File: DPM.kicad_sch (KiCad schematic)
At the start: 43 parts, among them J1 Conn_02x12_Odd_Even, J2 Conn_02x05_Odd_Even, U1 74LS251, U2 74LVC2G74, U25 74LS85, U28 74LS85, U3 ADG333A, U31 74LS85, U4 MCP23017_SP, U5 ADG333A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

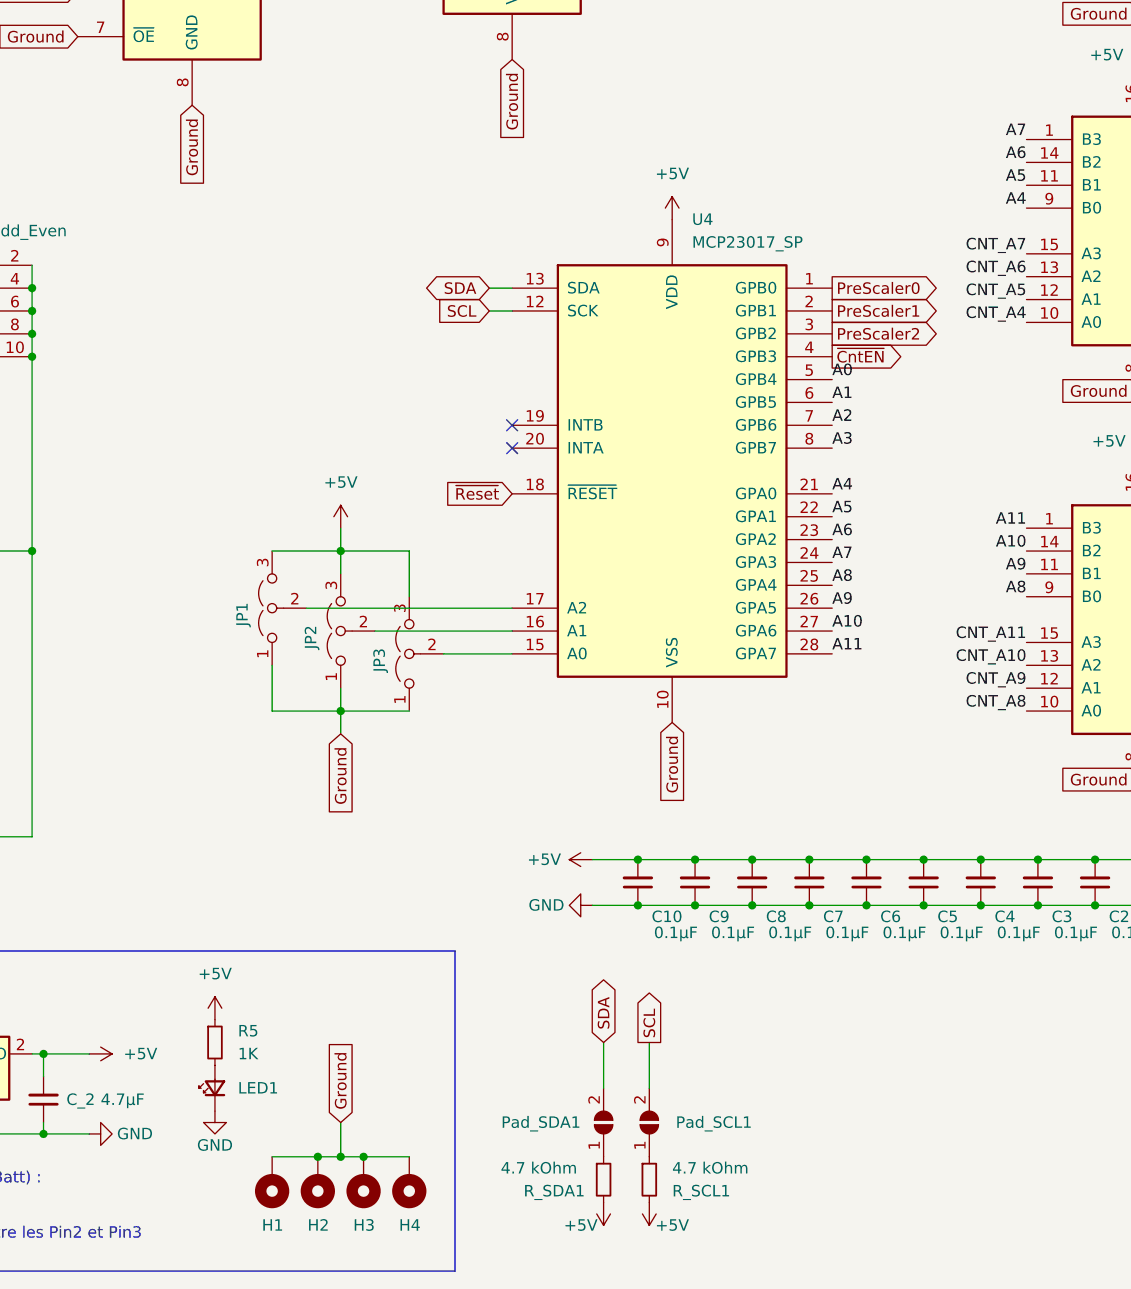
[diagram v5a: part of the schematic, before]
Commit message: Création modélisations sous Digital Correction routage des R SDA/SCL Ajout des screenshots de la carte
git-svn-id: file:///D%5C00%20-%20Dev%20&%20Calculs%5CRepoTortoiseSVN_PCB%5CD-DPM/trunk@25 f29d8339-a183-0348-962e-9e4594cf8312
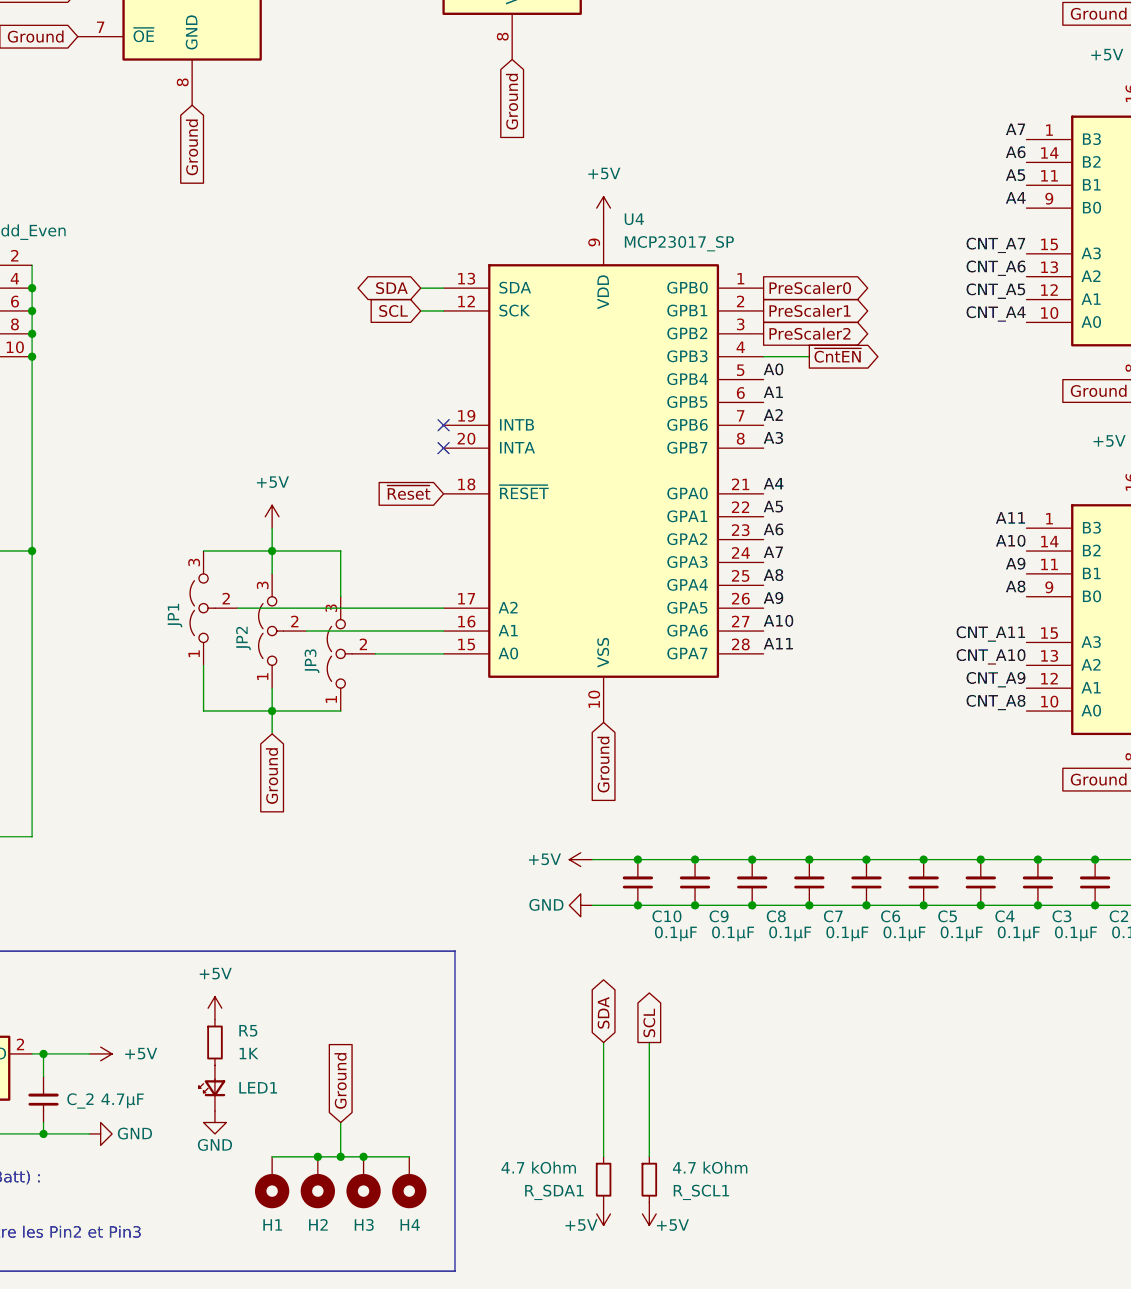
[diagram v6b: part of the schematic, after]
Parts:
- removed Pad_SCL1, Pad_SDA1: SolderJumper_2_Open, Jumper:SolderJumper-2_P1.3mm_Open_TrianglePad1.0x1.5mm, symbol Jumper:SolderJumper_2_Open
- R_SCL1, R_SDA1: footprint Resistor_SMD:R_1210_3225Metric_Pad1.30x2.65mm_HandSolder -> Resistor_THT:R_Axial_DIN0207_L6.3mm_D2.5mm_P10.16mm_Horizontal
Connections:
- net SCL: now also R_SCL1.1
- net SDA: now also R_SDA1.1
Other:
- moved on the sheet: JP1, JP2, JP3, U4
